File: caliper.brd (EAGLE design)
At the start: 70.1 x 50.5 mm, 57 parts, among them IC1 AT90S2313S, IC3 TS5205, IC6 MAX489CSD, Q10 BCX71SMD, Q11 BCX71SMD, Q12 BC817-40SMD, Q13 BC817-40SMD, Q2 BCX71SMD, Q3 BCX71SMD, Q4 BC817-40SMD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

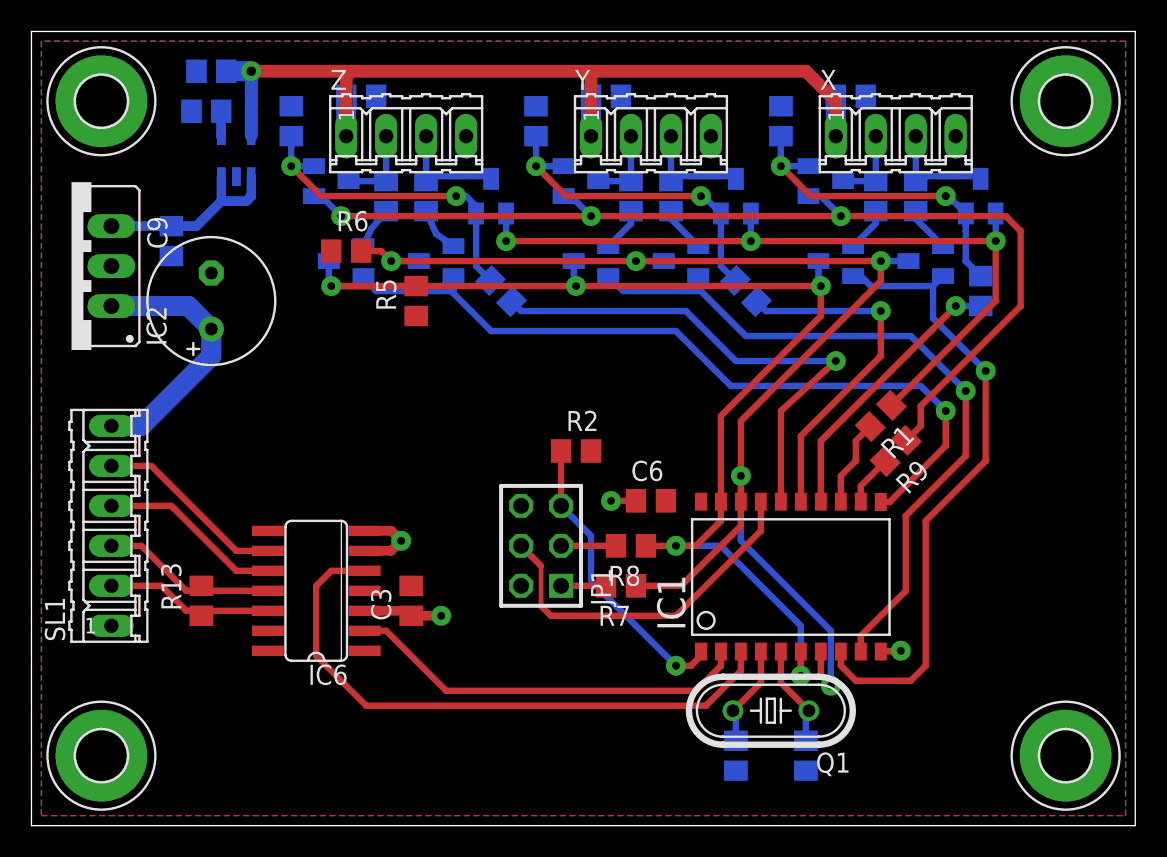
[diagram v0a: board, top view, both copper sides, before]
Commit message: switch to ATmega88 & spi readout, Board & schematic ready
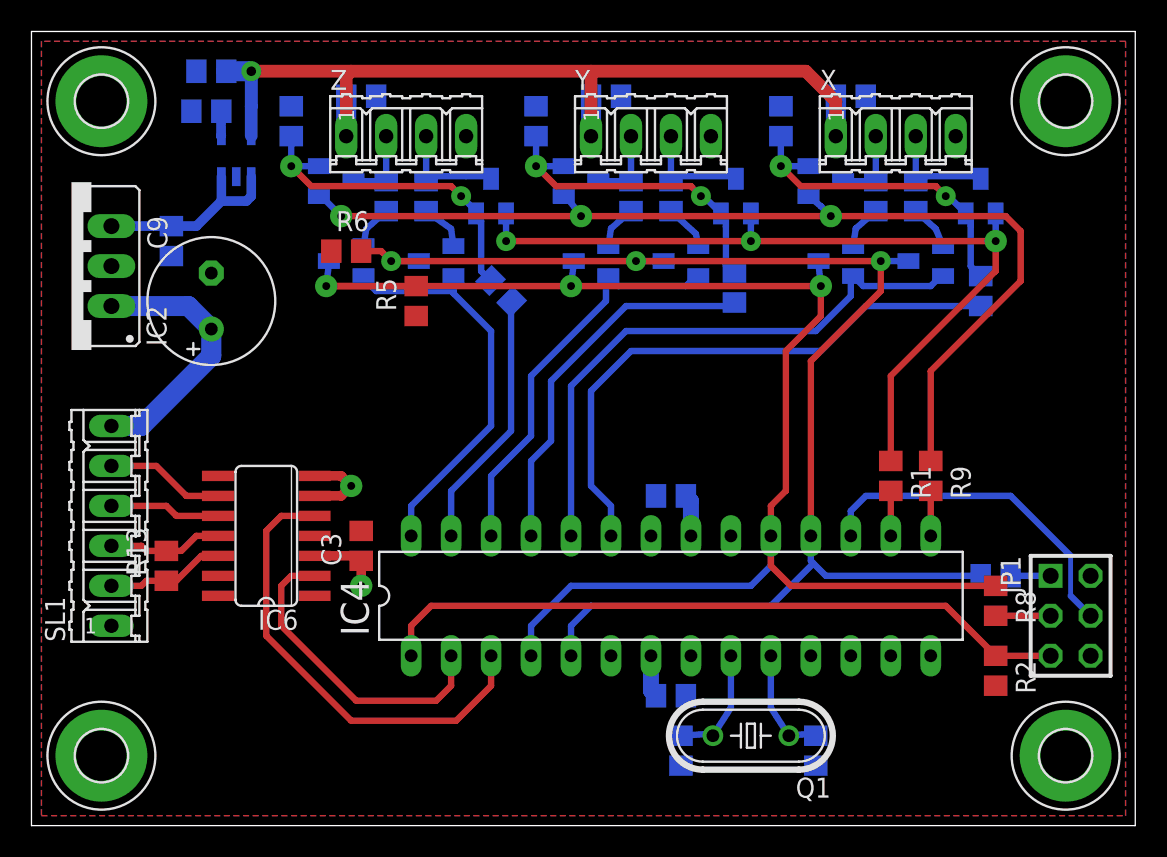
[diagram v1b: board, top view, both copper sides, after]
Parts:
- removed IC1: AT90S2313S, atmel:SO20L
- added C12: 100nF, rcl:C0805
- added IC4: ATMEGA48/88/168-PU, atmega8:DIL28-3
- moved JP1 33.9 mm to (66.0, 13.3), turned to 270 degrees
- moved R2 30.1 mm to (61.3, 9.84), turned to 270 degrees
- moved R7 23.8 mm to (61.3, 15.9), flipped to the bottom
- moved R8 23.4 mm to (61.3, 14.3), turned to 270 degrees
- moved C6 12.4 mm to (40.6, 8.26), flipped to the bottom
- moved C3 4.72 mm to (21.0, 17.8)
- moved IC6 4.72 mm to (14.9, 18.4)
- moved R1 3.86 mm to (54.6, 22.2), turned to 270 degrees
- moved C1 3.51 mm to (41.3, 4.76)
- moved R13 3.14 mm to (8.57, 16.5)
- moved R9 2.73 mm to (57.1, 22.2), turned to 270 degrees
- moved Q1 2.03 mm to (45.7, 5.71)
- moved R18 0.76 mm to (44.7, 34.2), turned to 270 degrees
- moved C2 0.71 mm to (49.8, 4.76)
- moved Q11 0.32 mm to (19.4, 41.0)
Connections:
- net !X_ENABLE: now also IC4.24; no longer IC1.8
- net !Y_ENABLE: now also IC4.26; no longer IC1.9
- net !Z_ENABLE: now also IC4.28; no longer IC1.11
- net +5V: now also C12.2, IC4.20, IC4.21, IC4.7; no longer IC1.20
- net DATA: now also IC4.18, IC4.5; no longer IC1.18, IC1.7
- net GND: now also C12.1, IC4.22, IC4.8; no longer IC1.10
- net MOSI: now also IC4.17; no longer IC1.17
- net N$1: now also IC4.9; no longer IC1.4
- net N$2: now also IC4.10; no longer IC1.5
- net N$3: now also IC4.2; no longer IC1.2
- net N$4: now also IC4.3; no longer IC1.3
- net N$6: now also IC4.15; no longer IC1.12
- net N$7: now also IC4.1; no longer IC1.1
- net N$8: now also IC4.16; no longer IC1.13
- net SCK: now also IC4.19, IC4.4; no longer IC1.19, IC1.6
- net X_MODE: now also IC4.23; no longer IC1.14
- net Y_MODE: now also IC4.25; no longer IC1.15
- net Z_MODE: now also IC4.27; no longer IC1.16
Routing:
- net N$7: track 18.8 -> 45.7 mm, vias 1 -> 0
- net !Z_ENABLE: track 49.7 -> 26.0 mm, vias 1 -> 0
- net !Y_ENABLE: track 46.1 -> 26.2 mm, vias 1 -> 0
- net X_MODE: track 17.6 -> 36.7 mm, vias 1 -> 0
- net SCK: track 79.2 -> 96.5 mm, vias 5 -> 3
- net Z_MODE: track 32.6 -> 16.5 mm, vias 1 -> 0
- net N$4: track 38.4 -> 29.5 mm
- net N$3: track 25.8 -> 20.0 mm
- net +5V: track 12.5 -> 17.8 mm
- net TX_P: track 12.2 -> 7.56 mm
- net TX_N: track 11.7 -> 7.03 mm
- net DATA: track 85.5 -> 89.6 mm, vias 5 -> 3
- net RX_N: track 11.4 -> 7.30 mm
- net !MODE: track 49.6 -> 53.1 mm
- net RX_P: track 10.9 -> 7.56 mm
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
